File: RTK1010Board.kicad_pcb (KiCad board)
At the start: 2 copper layers, 56.2 x 53.3 mm, 71 parts, among them J1 SMA, J2 IPEX, J3 USB_OTG, J4 BNO055, U1 RTK-1010, U2 MCP1700-3002E_SOT23, U3 MCP1700-3002E_SOT23, U4 ESP32-S2-WROVER

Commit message: some optimiziations implemented
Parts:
- added C12: 10uF, Capacitor_Tantalum_SMD:CP_EIA-7132-20_AVX-U_Pad2.72x3.50mm_HandSolder, F.Cu at (176.5, 123.8)
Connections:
- JP2 pad 2: 5V -> U5
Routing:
- net GND: track 352.8 -> 405.1 mm, vias 51 -> 59
- net U5: track 84.1 -> 107.0 mm, vias 2 -> 3
- net _GPIO26: track 20.9 -> 22.2 mm, vias 0 -> 1
- net ULNA: track 71.4 -> 70.9 mm, vias 3 -> 2

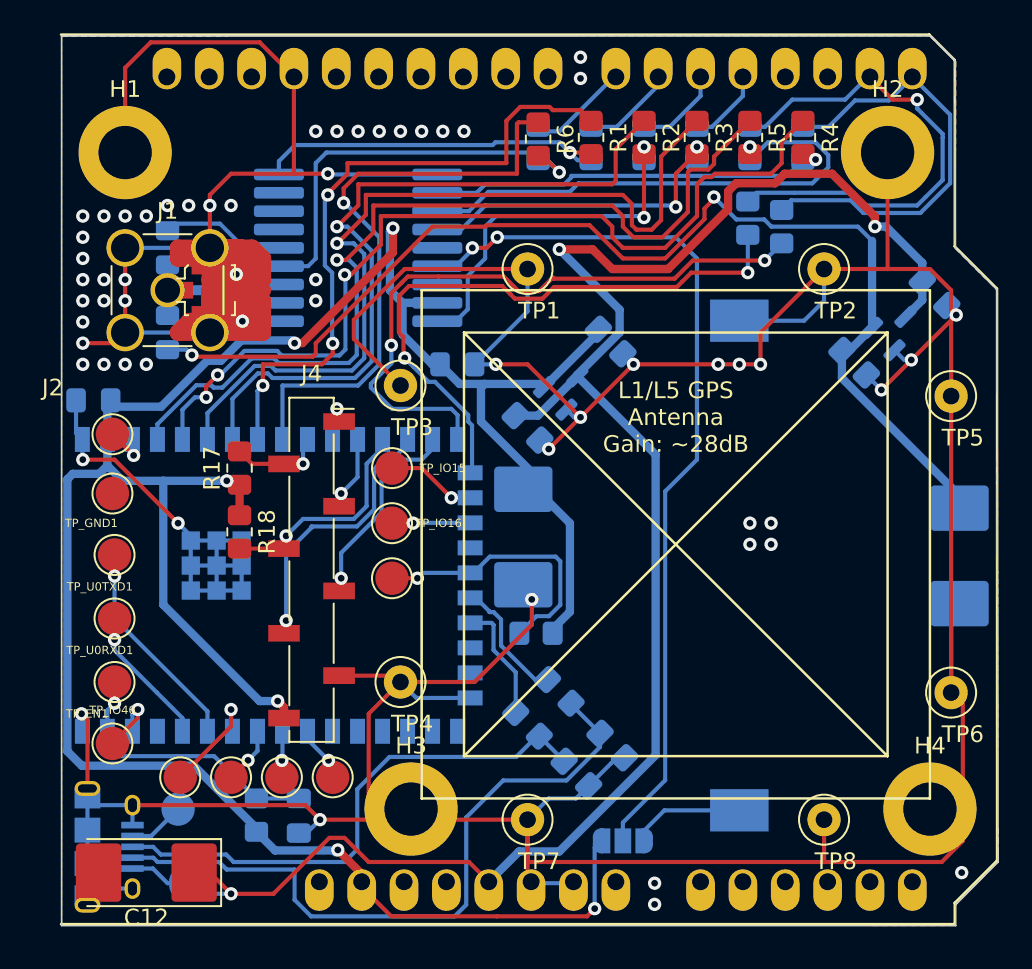
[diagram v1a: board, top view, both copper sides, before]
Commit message: RTK1010 VCC LP filter added
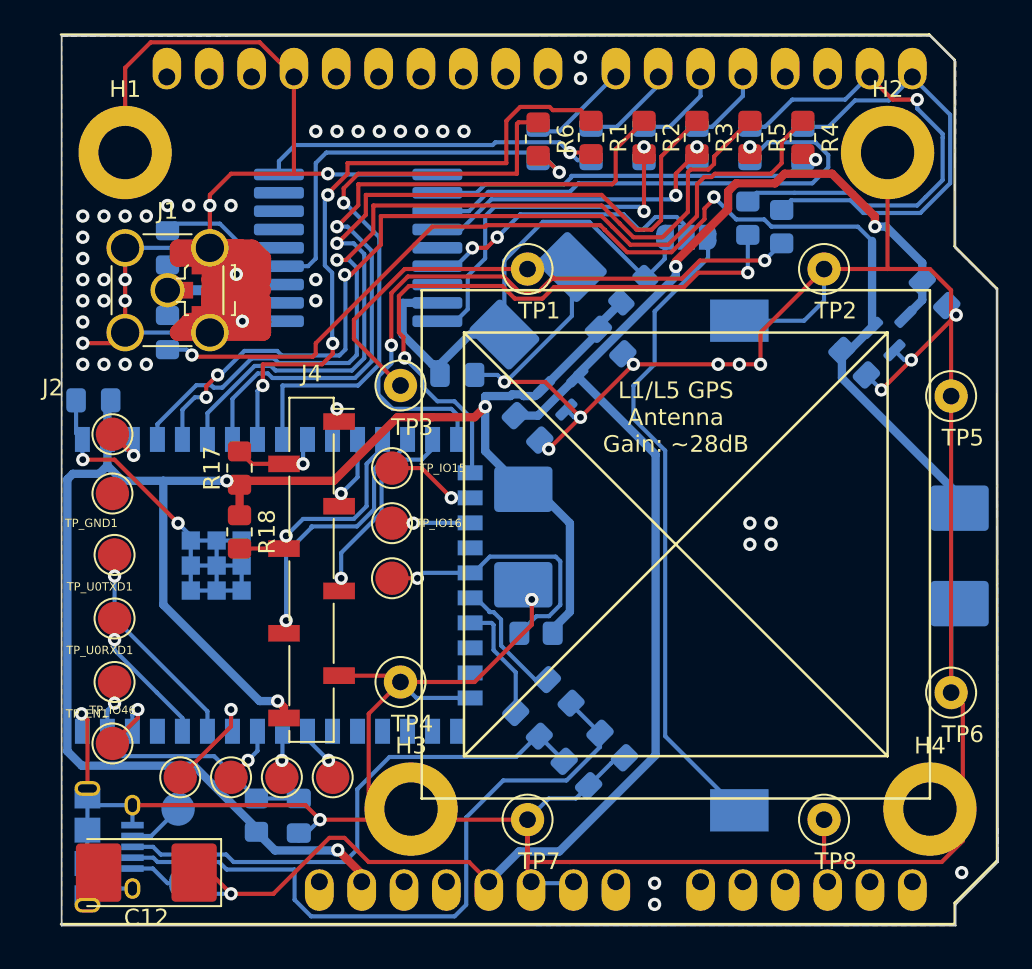
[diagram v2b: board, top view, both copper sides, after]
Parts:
- added C13: 10uF, Capacitor_Tantalum_SMD:CP_EIA-7132-20_AVX-U_Pad2.72x3.50mm_HandSolder, B.Cu at (200.0, 89.5)
- added L3: ?H, Inductor_SMD:L_0805_2012Metric_Pad1.15x1.40mm_HandSolder, B.Cu at (205.7, 88.9)
- moved JP1 36.4 mm to (208.9, 85.7)
- moved C5 0.64 mm to (195.2, 94.0)
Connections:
- C5 pad 1: +3V3 -> Net-(C13-Pad1)
- JP1 pad 1: +3V3 -> Net-(C13-Pad1)
- U1 pad 8: +3V3 -> Net-(C13-Pad1)
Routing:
- net +3V3: track 156.4 -> 118.4 mm, vias 6 -> 4
- net Net-(JP1-Pad2): track 53.0 -> 17.9 mm
- net Net-(BT1-Pad1): track 6.18 -> 38.8 mm
- net Net-(C13-Pad1): track 0.00 -> 30.6 mm
- net U5: track 107.0 -> 98.5 mm
- net GND: track 405.1 -> 409.1 mm
- net Net-(R3-Pad1): track 50.8 -> 50.0 mm
- net Net-(R4-Pad1): track 54.3 -> 53.8 mm

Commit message: Jefs comments implemented
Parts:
- moved C10 11.7 mm to (222.9, 93.3), turned to 45 degrees
- moved C6 1.36 mm to (222.8, 88.2)
- moved C7 1.36 mm to (218.0, 92.3)
- moved U3 1.36 mm to (220.4, 90.2)
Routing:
- net ULNA: track 70.6 -> 63.8 mm
- net GND: track 409.1 -> 404.1 mm, vias 59 -> 57
- net U5: track 98.5 -> 96.5 mm

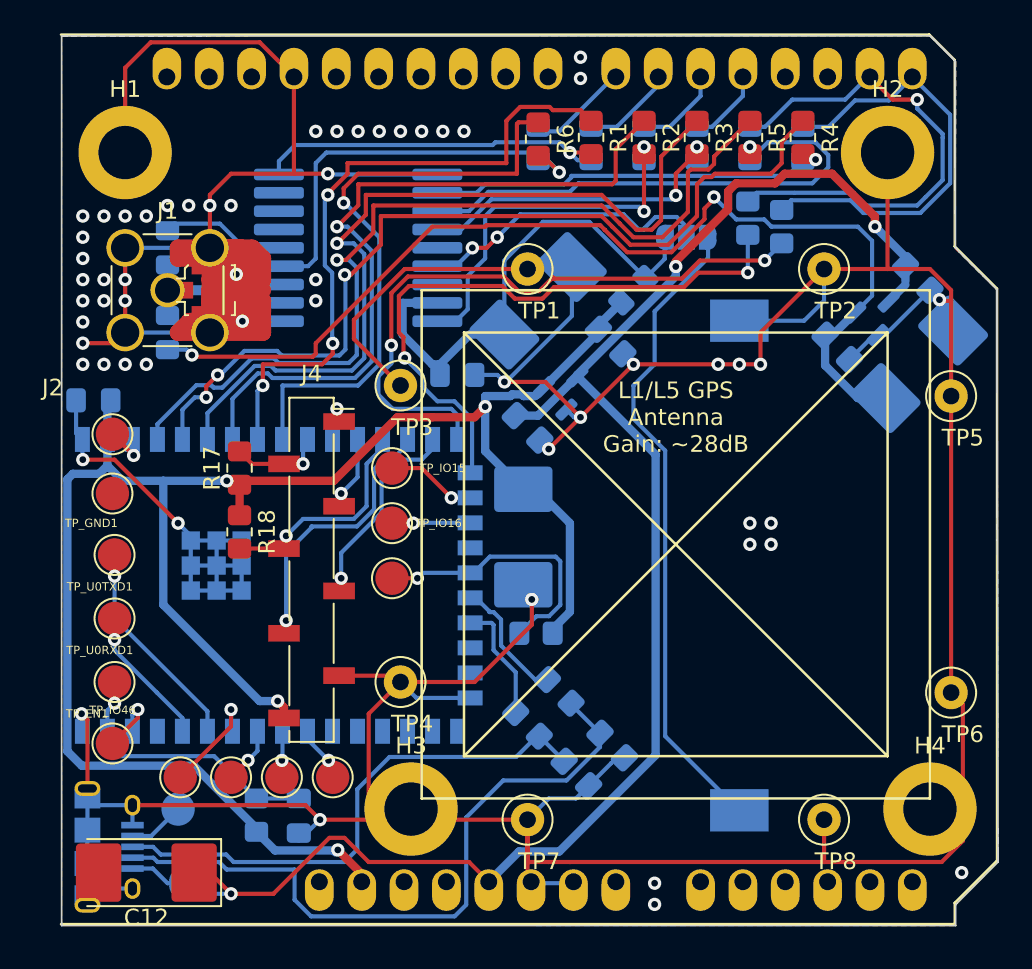
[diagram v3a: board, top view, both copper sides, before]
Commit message: some vias added
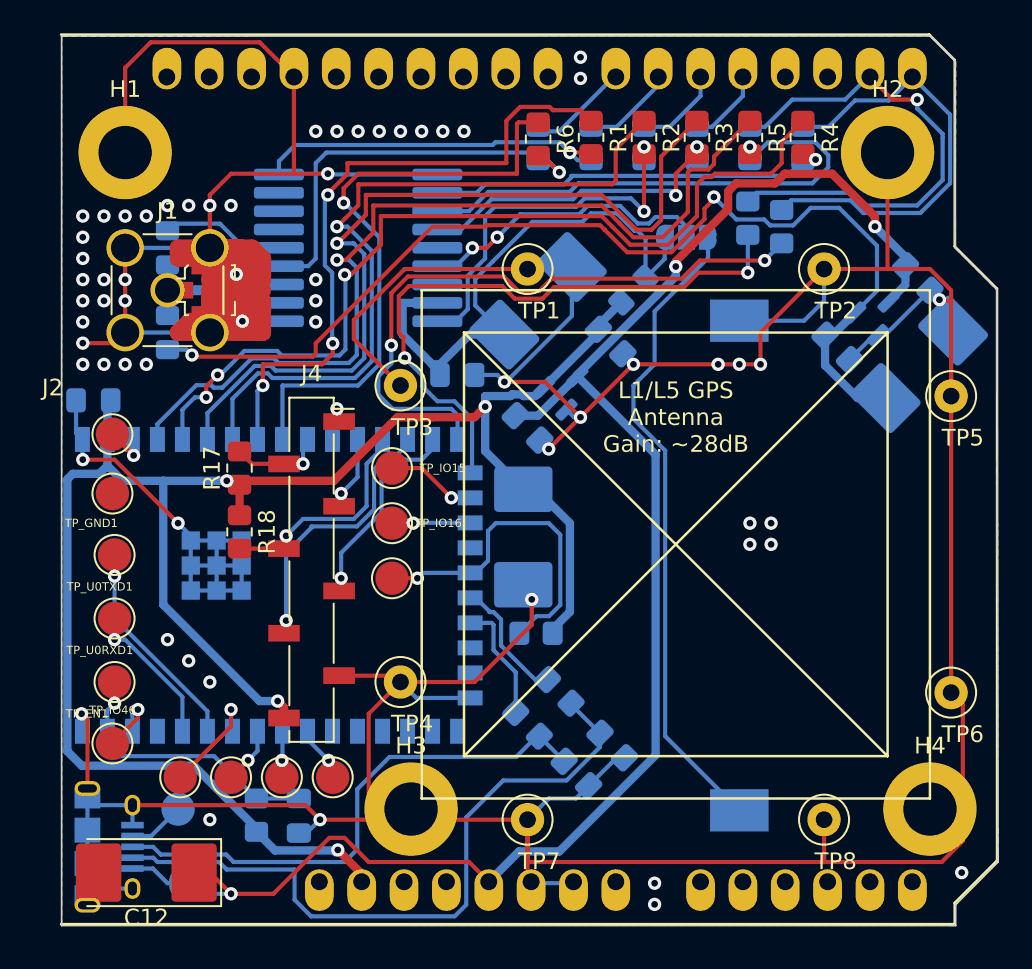
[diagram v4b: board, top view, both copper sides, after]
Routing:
- net Net-(R16-Pad2): track 16.8 -> 20.5 mm
- net Net-(C13-Pad1): track 30.6 -> 34.2 mm
- net ULNA: track 63.8 -> 64.9 mm
- net GND: vias 57 -> 62
